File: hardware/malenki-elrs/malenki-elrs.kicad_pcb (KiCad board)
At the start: 4 copper layers, 19 x 32 mm, 62 parts, among them J1 Conn_01x02_Male-Connector, J2 PROG Header, J3 Weapons, J4 Conn_01x02_Male-Connector, J5 Conn_01x02_Male-Connector, J6 Conn_01x02_Male-Connector, U1 SPX3819M5-L-3-3, U3 SX1280IMLTRT, U4 DRV8837DSGR, U5 DRV8837DSGR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

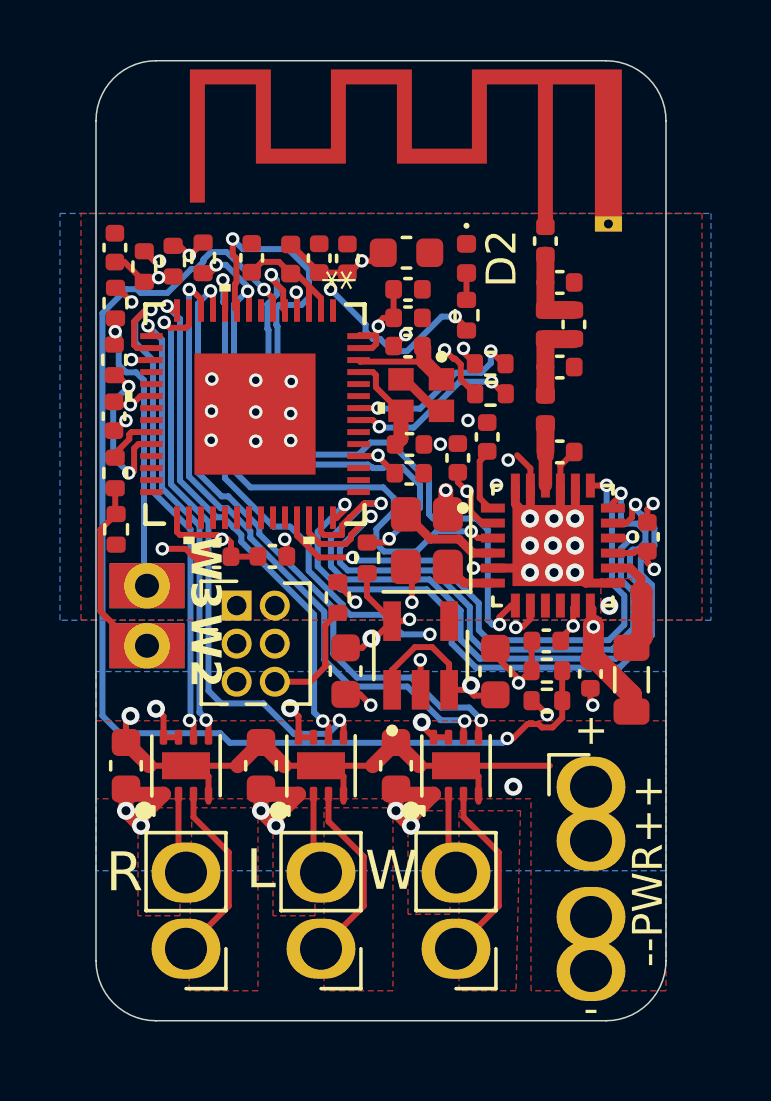
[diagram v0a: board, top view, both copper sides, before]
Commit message: Finalised pcb by placing ground stitching via's
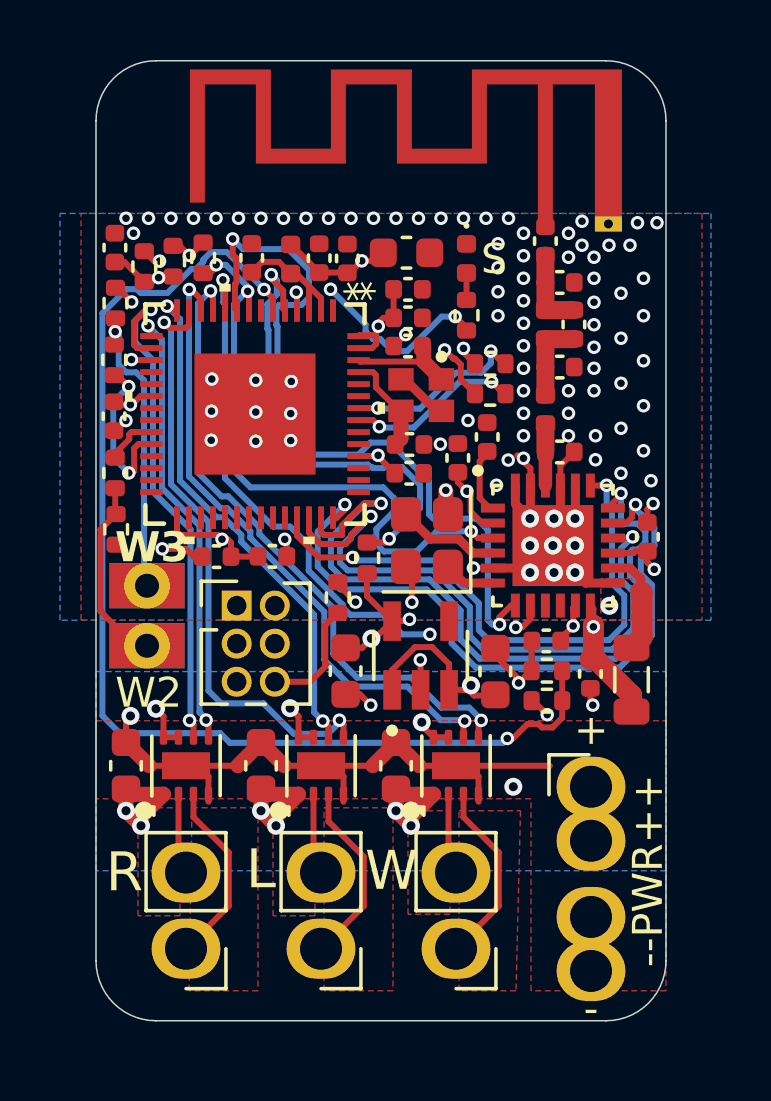
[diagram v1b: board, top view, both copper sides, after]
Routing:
- net GND: vias 38 -> 103
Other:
- board text added: "S"

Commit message: Generated production files
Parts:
- renumbered U7 to U2
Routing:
- net RADIO_NRESET: track 20.8 -> 21.9 mm
- net VSENSE: track 38.8 -> 39.6 mm

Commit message: Updated production files
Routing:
- net BUSY: track 25.8 -> 25.2 mm

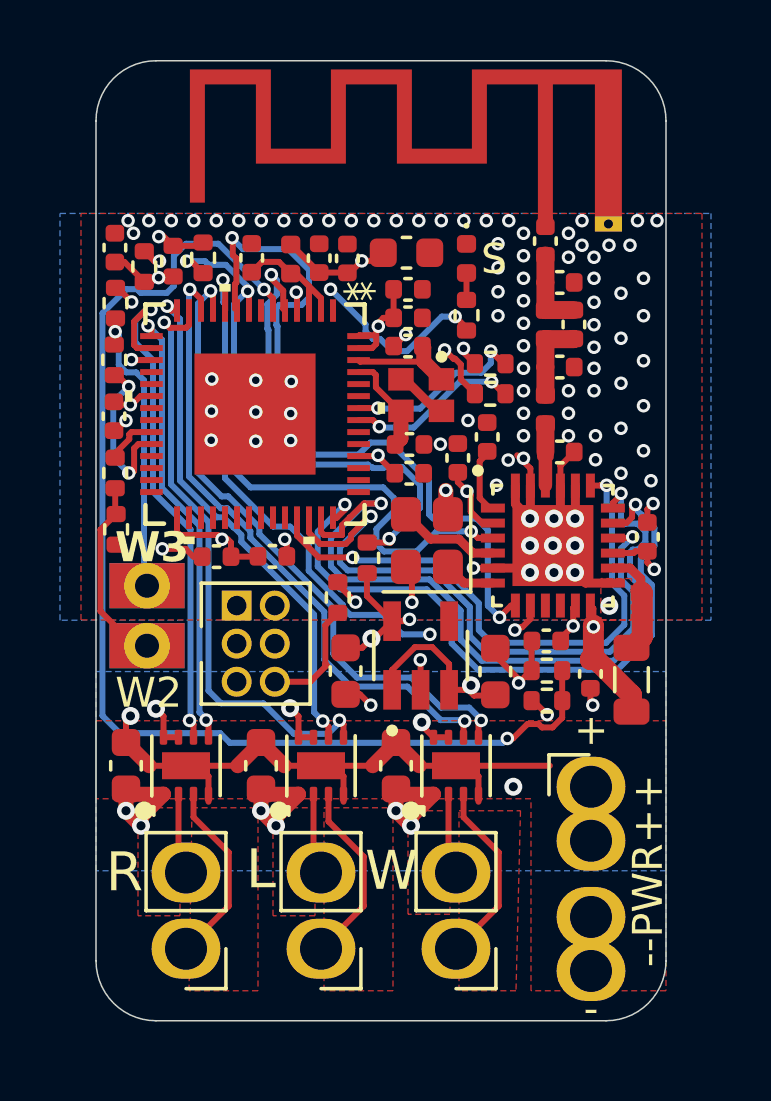
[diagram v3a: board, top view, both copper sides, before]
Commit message: Added power led, and images
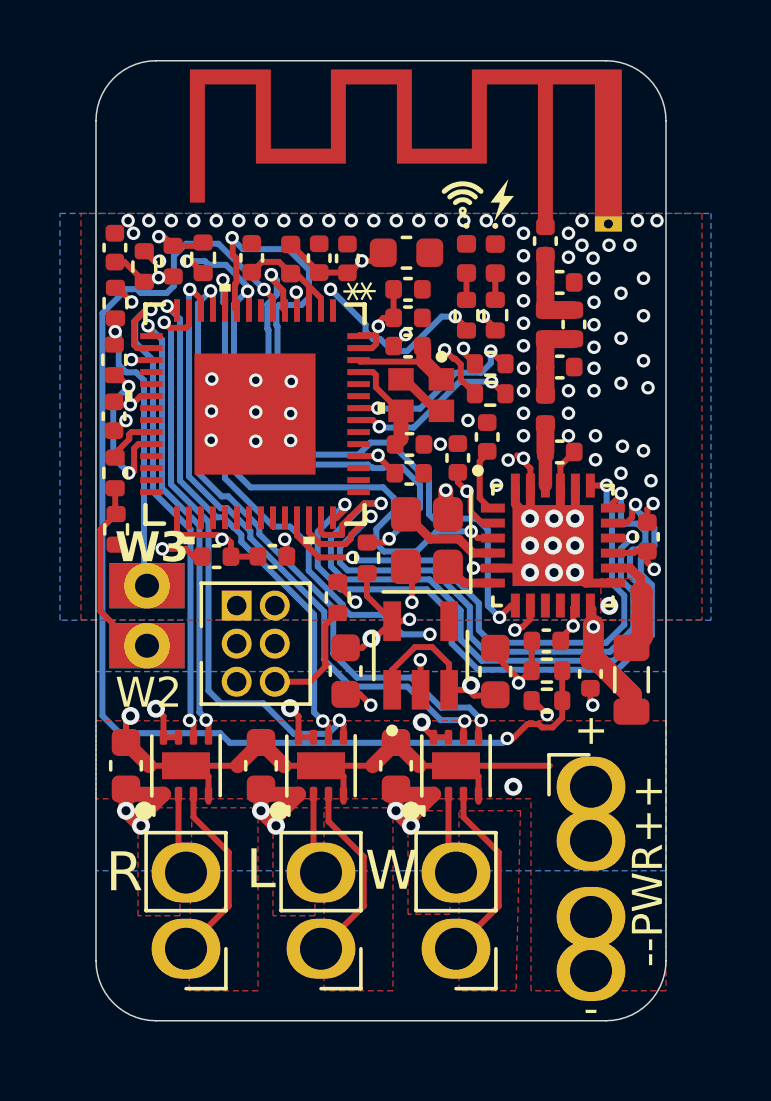
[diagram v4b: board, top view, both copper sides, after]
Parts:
- added D3: LED Red, LED_SMD:LED_0402_1005Metric, F.Cu at (101.3, 56.1)
- added G***: LOGO, LOGO, F.Cu at (101.5, 54.2)
- added G***: LOGO, LOGO, F.Cu at (97.5, 66.2)
- added G***: LOGO, LOGO, F.Cu at (100.2, 54.1)
- added G***: LOGO, LOGO, B.Cu at (90.7, 52.1)
- added R16: 470, Resistor_SMD:R_0402_1005Metric, F.Cu at (101.3, 58.0)
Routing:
- net Net-(D3-A): track 0.00 -> 0.89 mm
- net VLOGIC: track 27.4 -> 28.1 mm, vias 13 -> 14
- net GND: vias 103 -> 99
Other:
- board text removed: "S"
